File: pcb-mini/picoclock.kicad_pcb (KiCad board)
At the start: 4 copper layers, 140 x 54 mm, 136 parts, among them J1 UART, J10 USB, J11 Alt Power, J12 LED_5V, J13 ESP32_IO0, J14 SJ2-35863B1-SMT-TR, J15 Conn_01x24, J2 USB_A, J3 UART, J4 xx, J5 Micro_SD_Card_Det1, J6 USB_C_Receptacle, J8 Conn_01x21_Pin, J9 AUDIO, Q1 BSS138, Q3 BSS138, SW1 SW_Push, SW2 SW_Push, SW3 SW_Push, SW4 SW_Push, SW5 SW_Push, SW6 SW_Push, SW7 SW_Push, U1 PCF8563T, U10 74LS157, U2 RP2350_80QFN, U3 MCP9808_MSOP, U4 PCM5100, U5 PAM8302A, U6 W25Q128JVS, U7 MCP45X1-104E, U8 NCP1117-3.3_SOT223, U9 ESP32-WROOM-E, Y1 Crystal, Y2 ABM8-272-T3

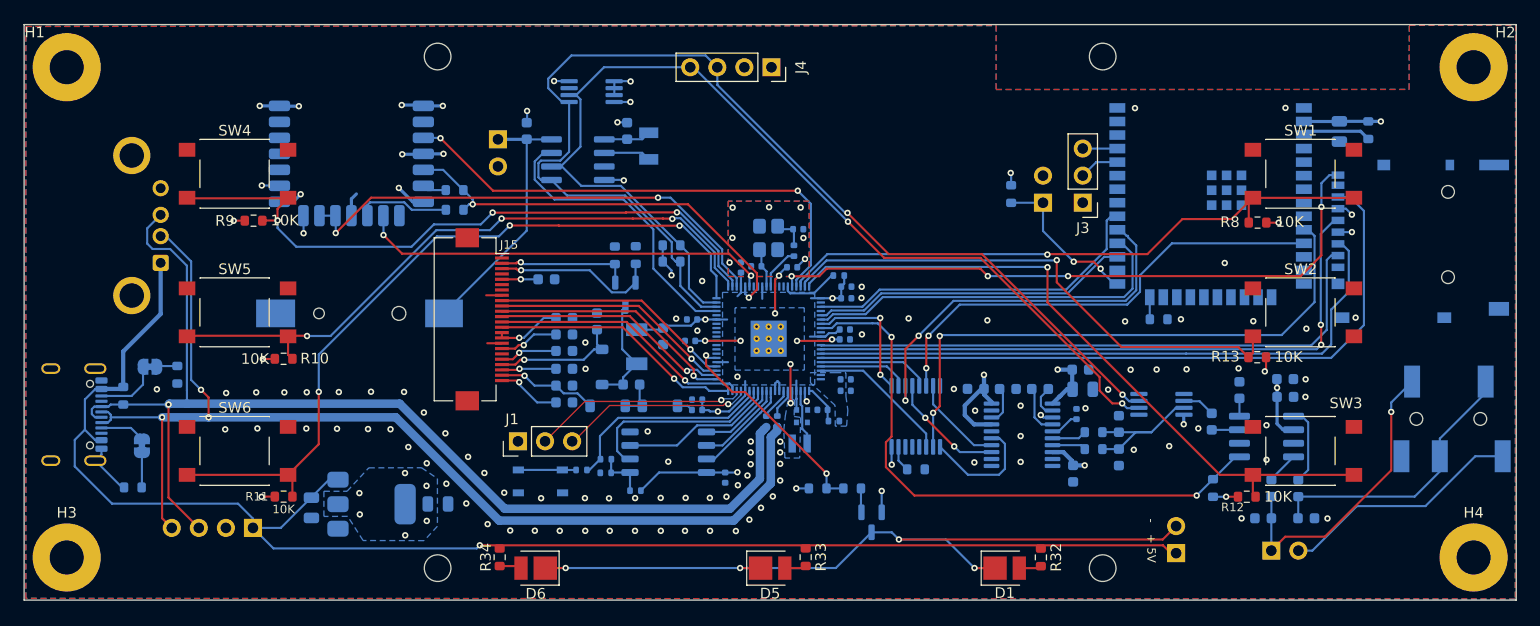
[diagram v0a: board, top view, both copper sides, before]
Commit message: [pcb] mini: many silkscreen fixes
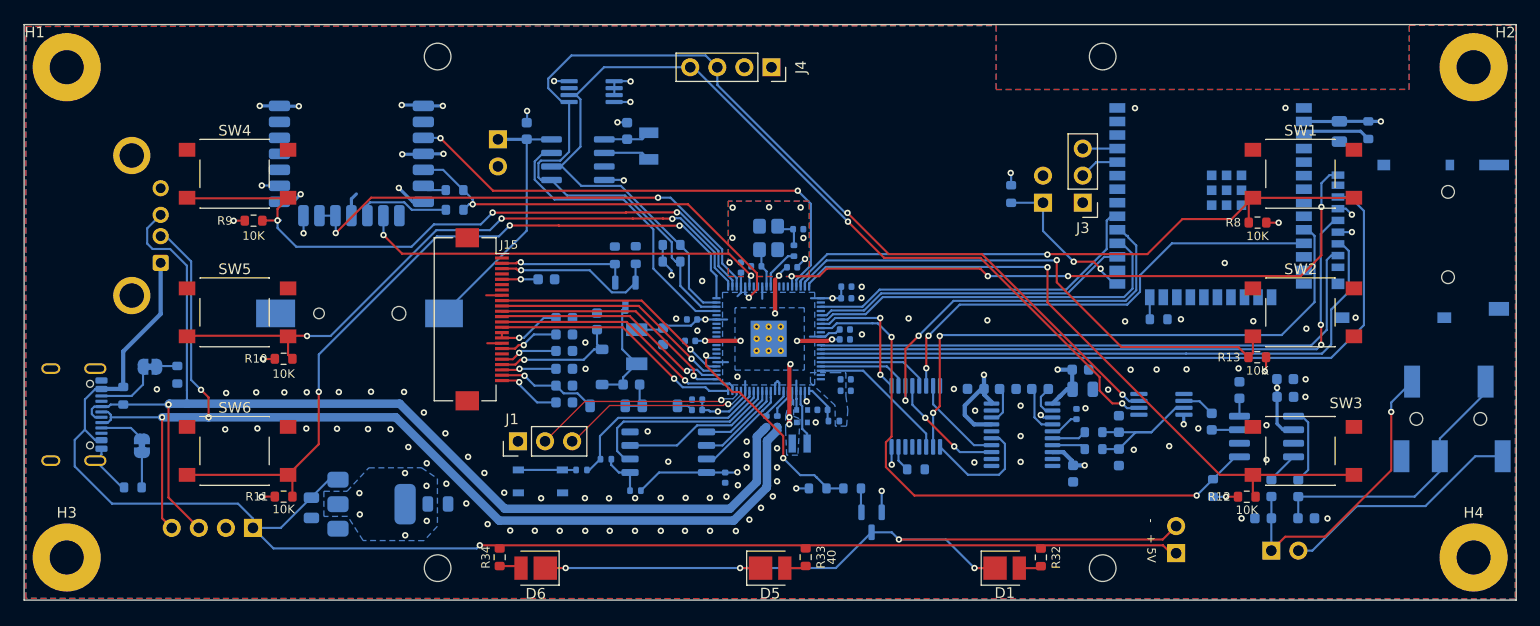
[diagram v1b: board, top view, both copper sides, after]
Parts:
- removed R18: 1k, Resistor_SMD:R_0402_1005Metric
- removed R20: DNF, Resistor_SMD:R_0402_1005Metric
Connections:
- U2 pad 9: GPIO11/irq -> unconnected-(U2-GPIO11-Pad9)
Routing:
- net +1V1: track 21.4 -> 27.2 mm, vias 8 -> 9
- net /uC/RUN: track 5.48 -> 0.00 mm
- net +3V3: track 97.4 -> 96.2 mm
- net GND: vias 119 -> 118

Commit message: [pcb] mini: add RGB leds
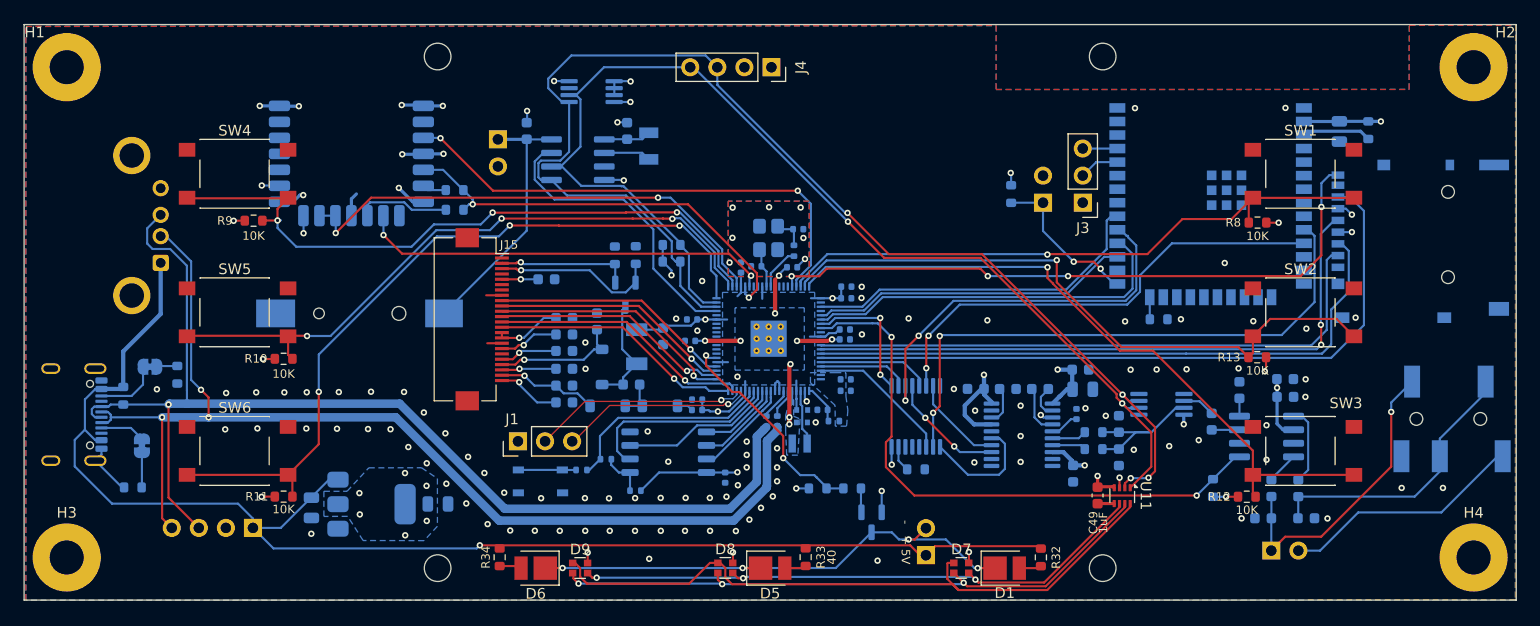
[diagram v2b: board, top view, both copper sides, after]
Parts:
- added C49: 1uF, Capacitor_SMD:C_0603_1608Metric, F.Cu at (180.7, 124.2)
- added D7: LED_RGBA, Resistor_SMD:R_Array_Convex_2x0606, F.Cu at (167.9, 131.0)
- added D8: LED_RGBA, Resistor_SMD:R_Array_Convex_2x0606, F.Cu at (145.8, 131.0)
- added D9: LED_RGBA, Resistor_SMD:R_Array_Convex_2x0606, F.Cu at (132.2, 131.0)
- added U11: ~, Lunasys_Library:LP5817, F.Cu at (183.0, 124.2)
- moved J12 23.5 mm to (164.6, 129.8)
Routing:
- net Net-(D7-RK): track 0.00 -> 63.1 mm
- net Net-(D7-GK): track 0.00 -> 58.6 mm, vias 0 -> 3
- net Net-(D7-BK): track 0.00 -> 55.7 mm, vias 0 -> 3
- net LED_5V-: track 73.4 -> 48.7 mm
- net SDA: track 107.9 -> 120.1 mm, vias 2 -> 4
- net LED_5V+: track 143.1 -> 131.0 mm
- net GPIO9/btn: track 50.0 -> 60.8 mm
- net SCL: track 99.7 -> 109.1 mm
- net +3V3: track 96.2 -> 101.9 mm, vias 31 -> 35
- net GND: track 43.3 -> 46.1 mm, vias 118 -> 124
- net +1V1: track 27.2 -> 25.5 mm

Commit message: [pcb] mini: fix I2S switch footprint, many small tweaks
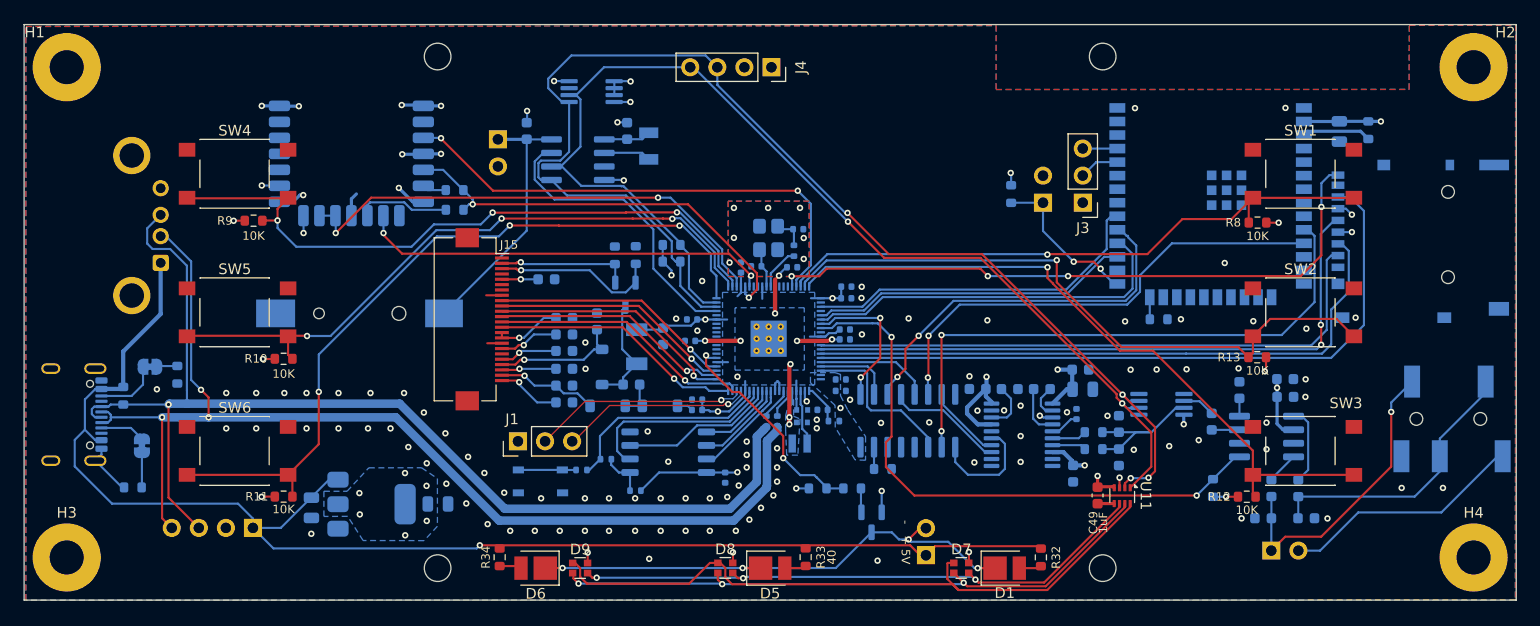
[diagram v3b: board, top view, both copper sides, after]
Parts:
- U10: footprint Package_SO:TSSOP-16_4.4x5mm_P0.65mm -> Package_SO:SOIC-16_3.9x9.9mm_P1.27mm
- moved R30 3.11 mm to (160.6, 121.7)
- moved U10 0.85 mm to (162.9, 117.2)
- moved C41 0.47 mm to (156.6, 114.4)
- moved C45 0.47 mm to (156.6, 113.3)
- moved C7 0.18 mm to (175.5, 114.2)
- moved C3 0.18 mm to (169.5, 114.2)
- moved C9 0.18 mm to (172.5, 114.2)
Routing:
- net +3V3: track 101.9 -> 99.5 mm
- net PICO_LRCK: track 13.6 -> 15.4 mm
- net /DIN: track 8.79 -> 7.14 mm
- net GND: track 46.1 -> 44.5 mm, vias 124 -> 129
- net BT_I2S_SCK: track 36.8 -> 35.6 mm
- net PICO_BCK: track 8.47 -> 7.29 mm
- net GPIO35_I2S_SELECT: track 12.6 -> 13.8 mm
- net Net-(U4-LDOO): track 3.59 -> 4.64 mm
- net BT_I2S_SDATA: track 44.5 -> 45.3 mm
- net BT_I2S_LRCK: track 54.6 -> 53.9 mm
- net /LRCK: track 11.2 -> 10.6 mm
- net /BCK: track 11.0 -> 11.6 mm, vias 2 -> 0

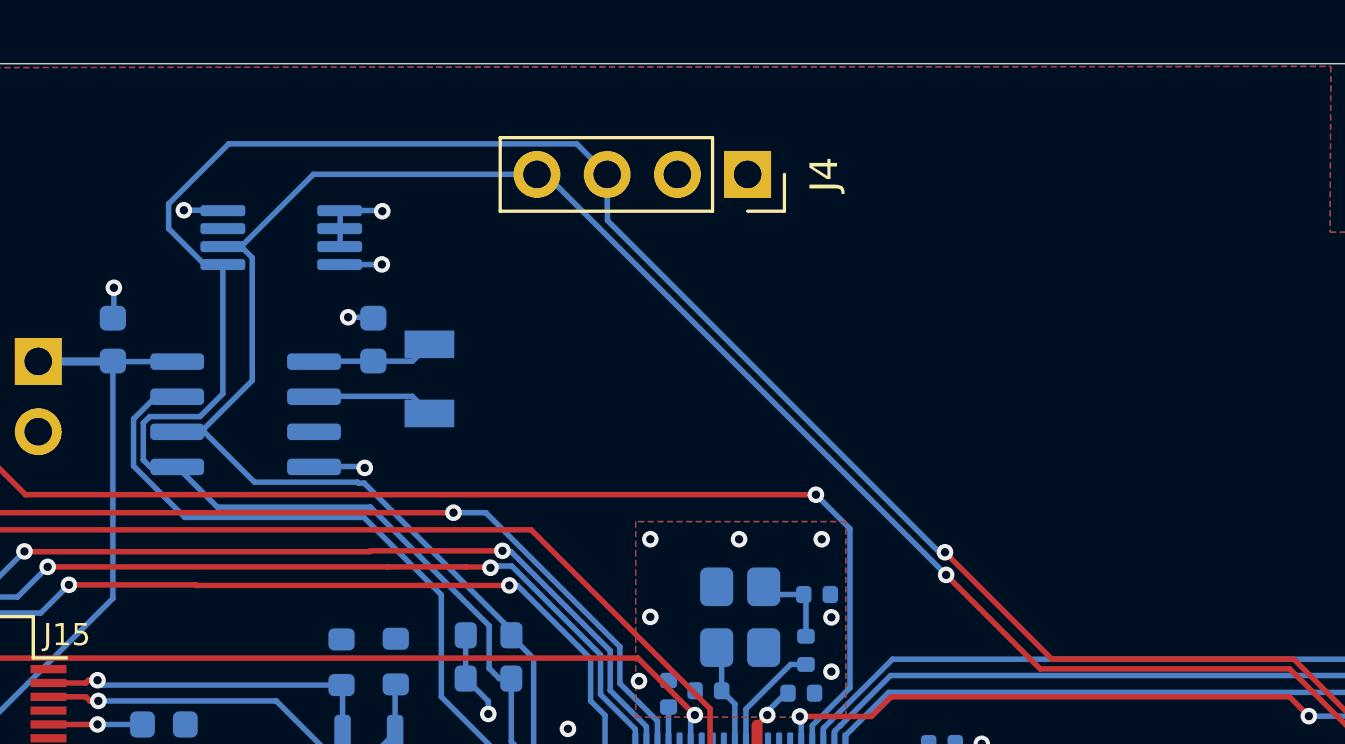
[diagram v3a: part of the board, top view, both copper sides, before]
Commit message: [pcn] mini: isolate temp sensor
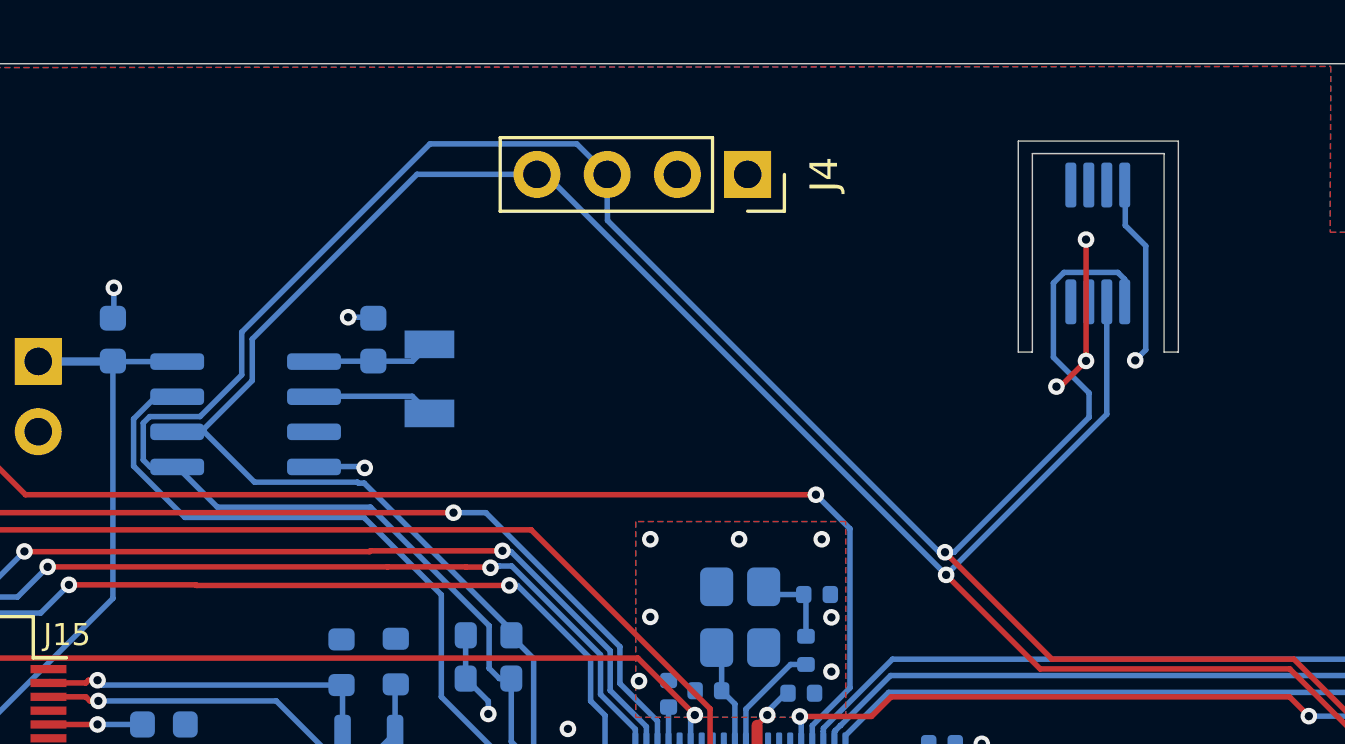
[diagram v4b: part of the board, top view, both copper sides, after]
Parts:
- moved U3 29.5 mm to (162.8, 86.5), turned to 90 degrees
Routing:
- net SDA: track 120.1 -> 130.1 mm
- net SCL: track 109.1 -> 118.2 mm
- net +3V3: track 99.5 -> 104.8 mm
- net GND: track 44.5 -> 46.0 mm, vias 129 -> 130
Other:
- outline, holes or cut-outs redrawn

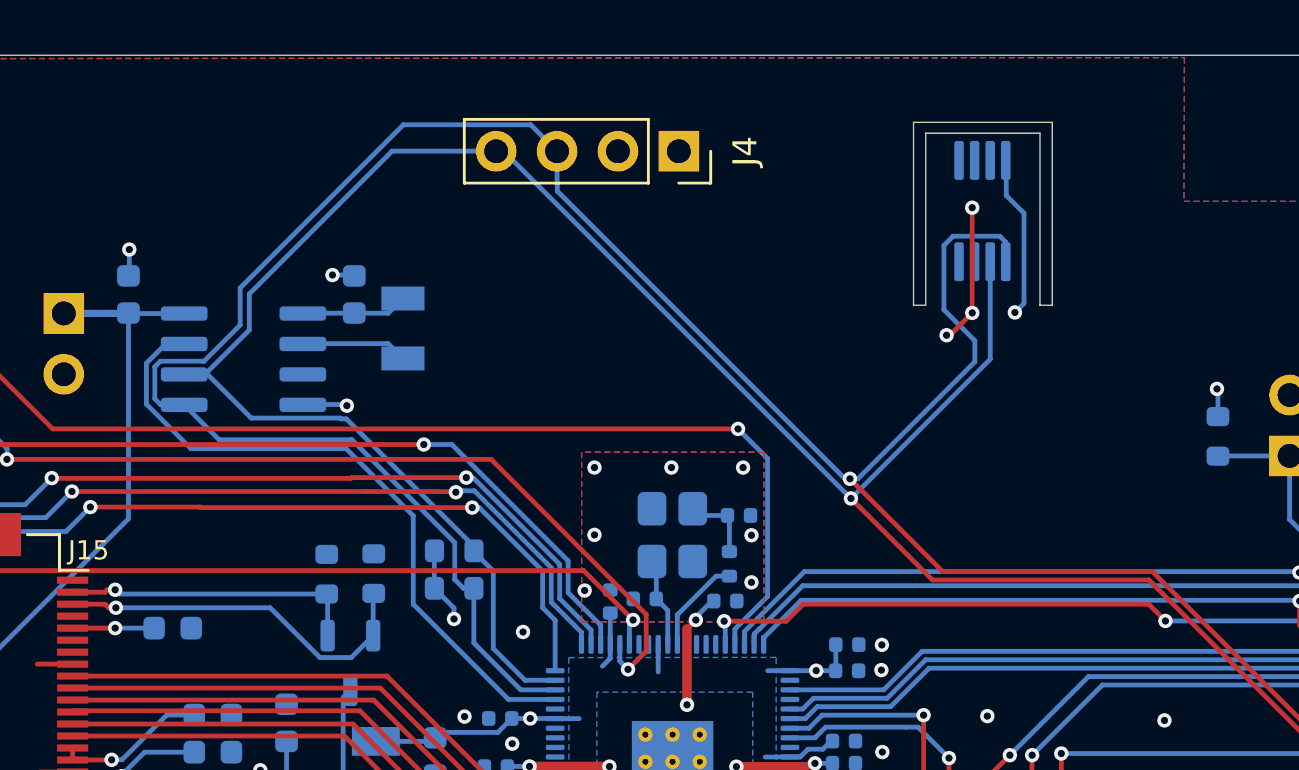
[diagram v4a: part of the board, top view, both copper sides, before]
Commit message: [pcb] mini: add ENS160 gaz sensor
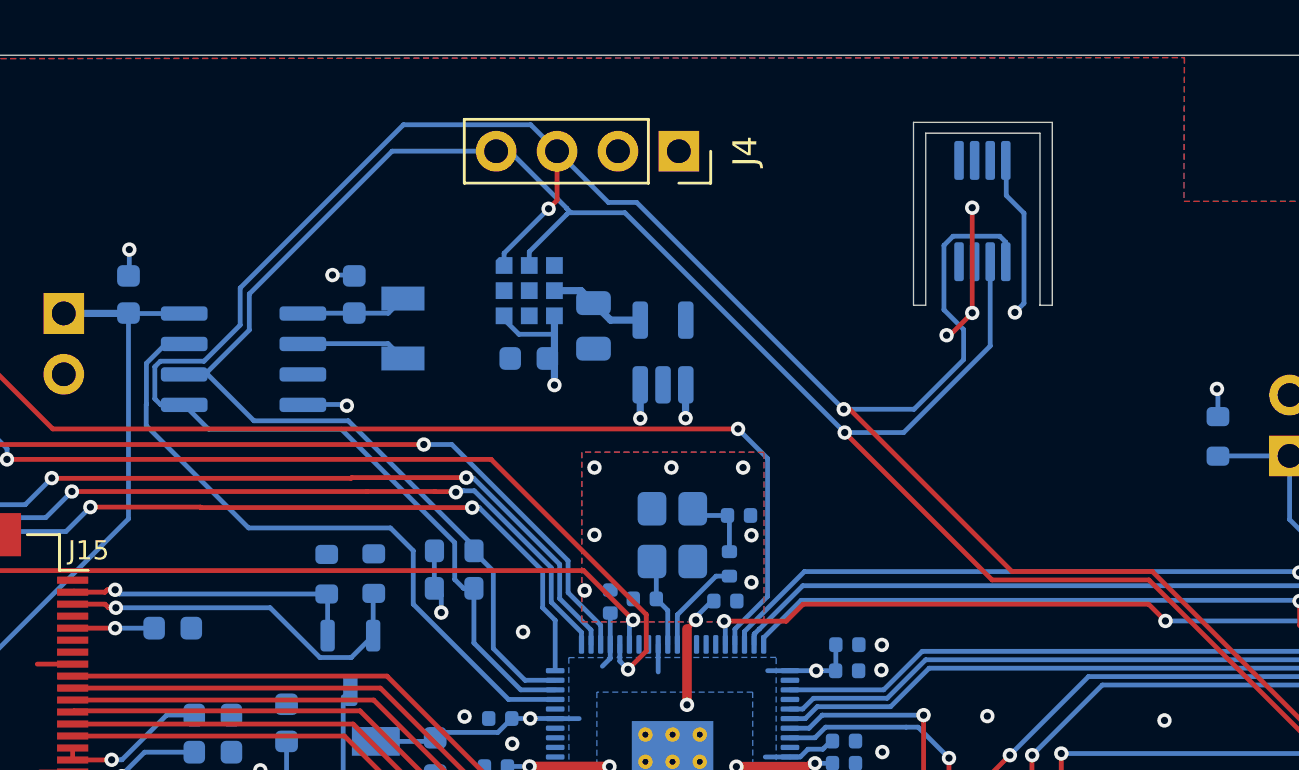
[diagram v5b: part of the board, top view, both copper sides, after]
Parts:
- added C50: 10u, Capacitor_SMD:C_0805_2012Metric, B.Cu at (146.6, 91.3)
- added C51: 0.1uF, Capacitor_SMD:C_0603_1608Metric, B.Cu at (143.9, 92.7)
- added U12: ENS160, ENS160:ENS160, B.Cu at (143.9, 89.8)
- added U13: TCR2EE19, Package_TO_SOT_SMD:SOT-23-5_HandSoldering, B.Cu at (149.5, 92.4)
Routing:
- net +3V3: track 104.8 -> 112.5 mm, vias 35 -> 38
- net Net-(U12-Vdd): track 0.00 -> 4.09 mm
- net SDA: track 130.1 -> 133.1 mm, vias 4 -> 5
- net SCL: track 118.2 -> 120.0 mm
